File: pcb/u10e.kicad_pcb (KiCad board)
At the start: 2 copper layers, 57 parts, among them J1 MJ-4PP-9, K11 KEYSW, K12 KEYSW, K13 KEYSW, K14 KEYSW, K15 KEYSW, K16 KEYSW, K21 KEYSW, K22 KEYSW, K23 KEYSW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

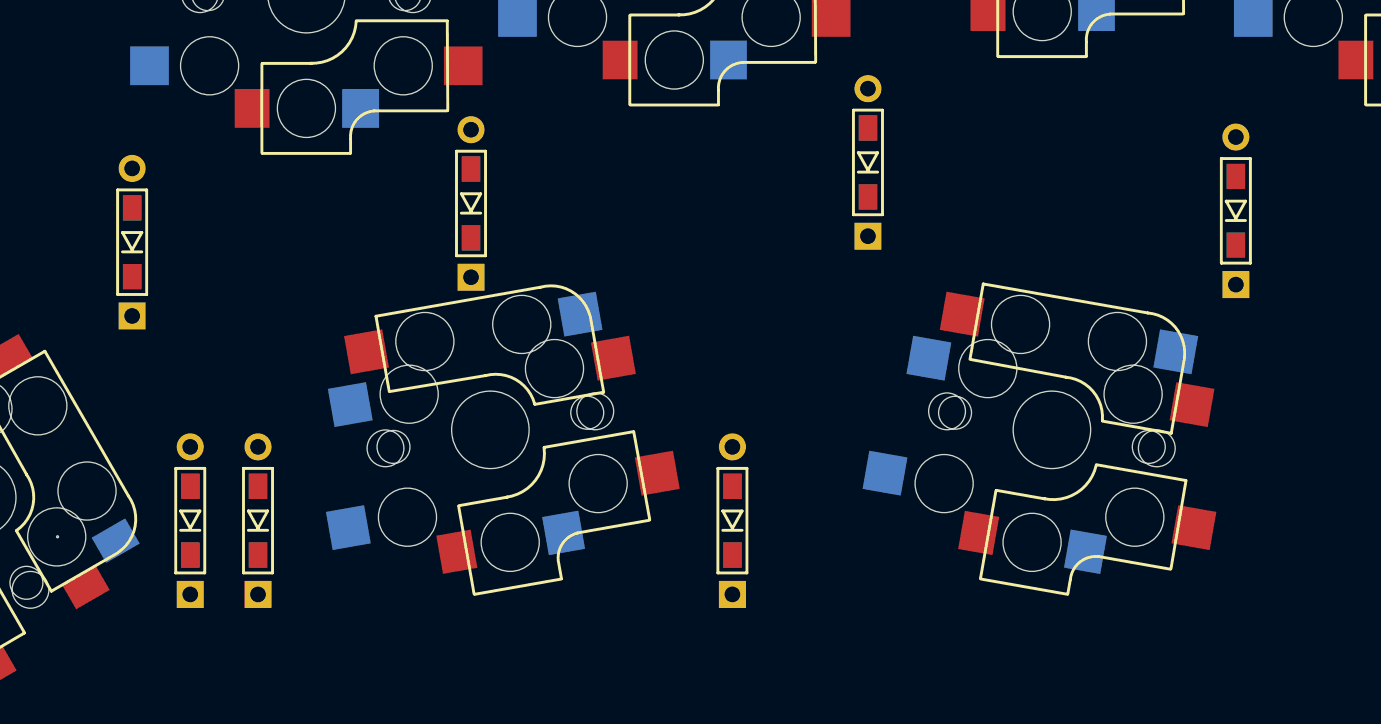
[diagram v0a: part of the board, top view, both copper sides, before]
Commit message: moved bottom row to more evenly distribute x space
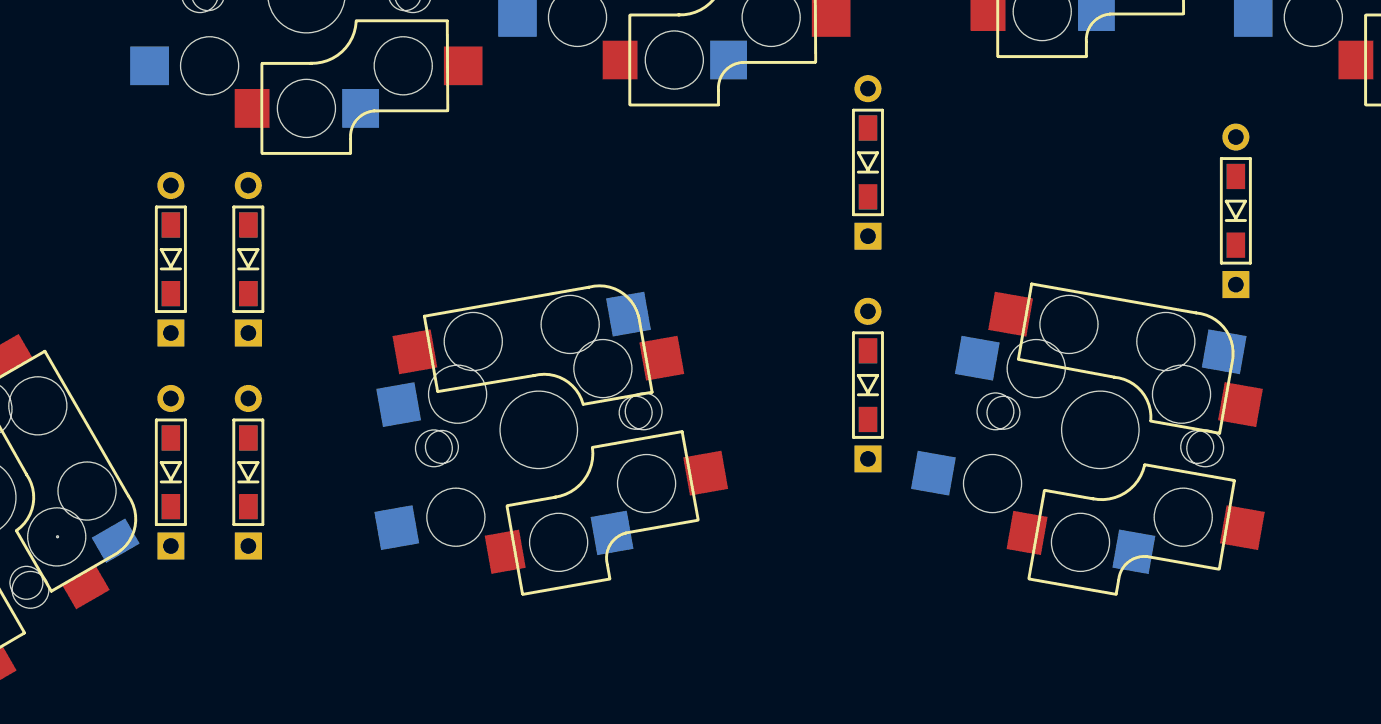
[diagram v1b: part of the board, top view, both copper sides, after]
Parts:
- moved D42 11.9 mm to (62.0, 98.7)
- moved D53 9.90 mm to (94.0, 105.2)
- moved D51 2.69 mm to (58.0, 109.7)
- moved D52 2.55 mm to (62.0, 109.7)
- moved K52 2.50 mm to (77.0, 107.5)
- moved K53 2.50 mm to (106.0, 107.5)
- moved D41 2.19 mm to (58.0, 98.7)

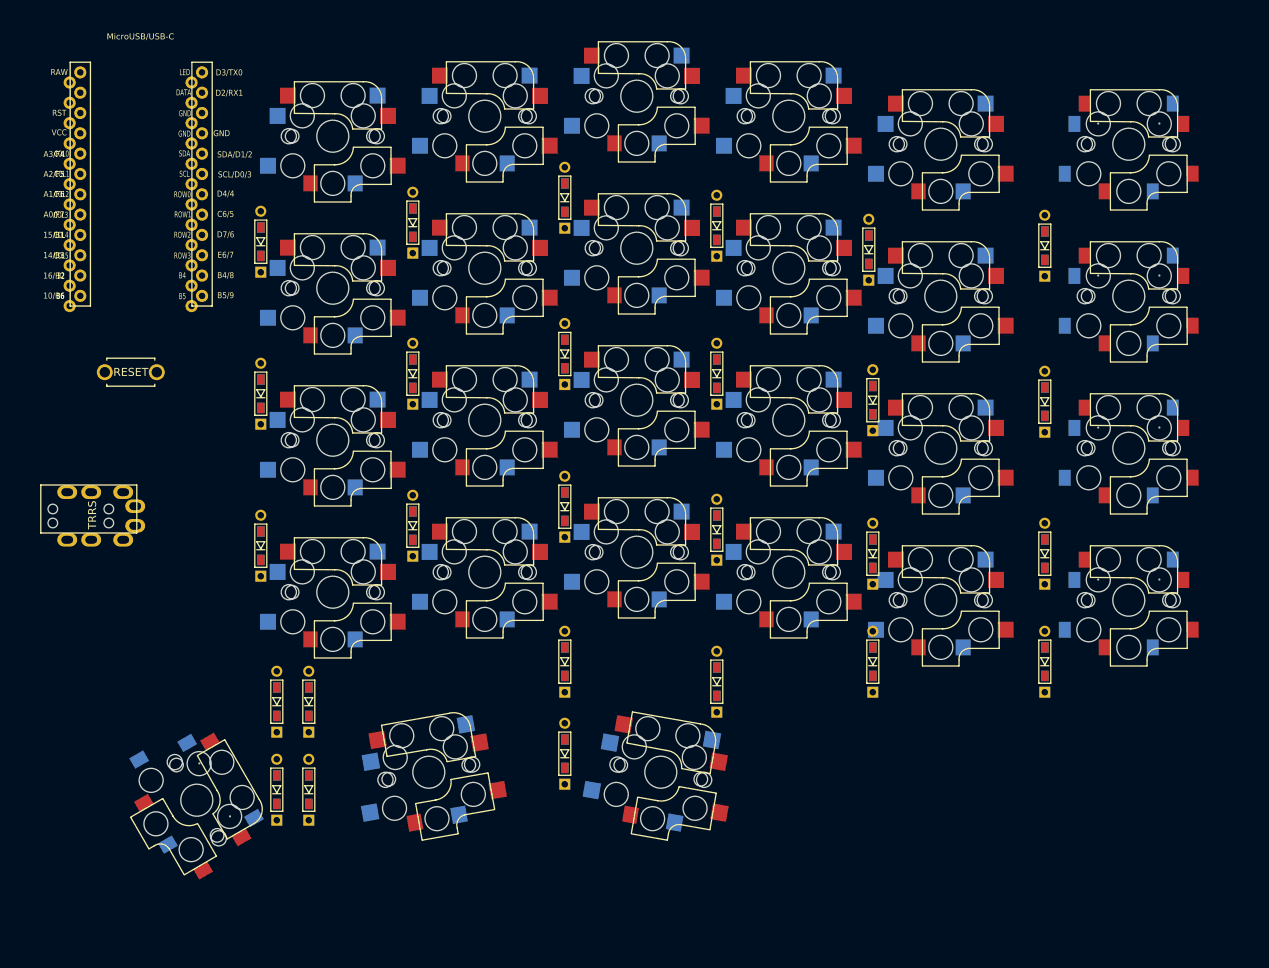
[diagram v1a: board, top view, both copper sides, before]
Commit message: added r1 edgecuts
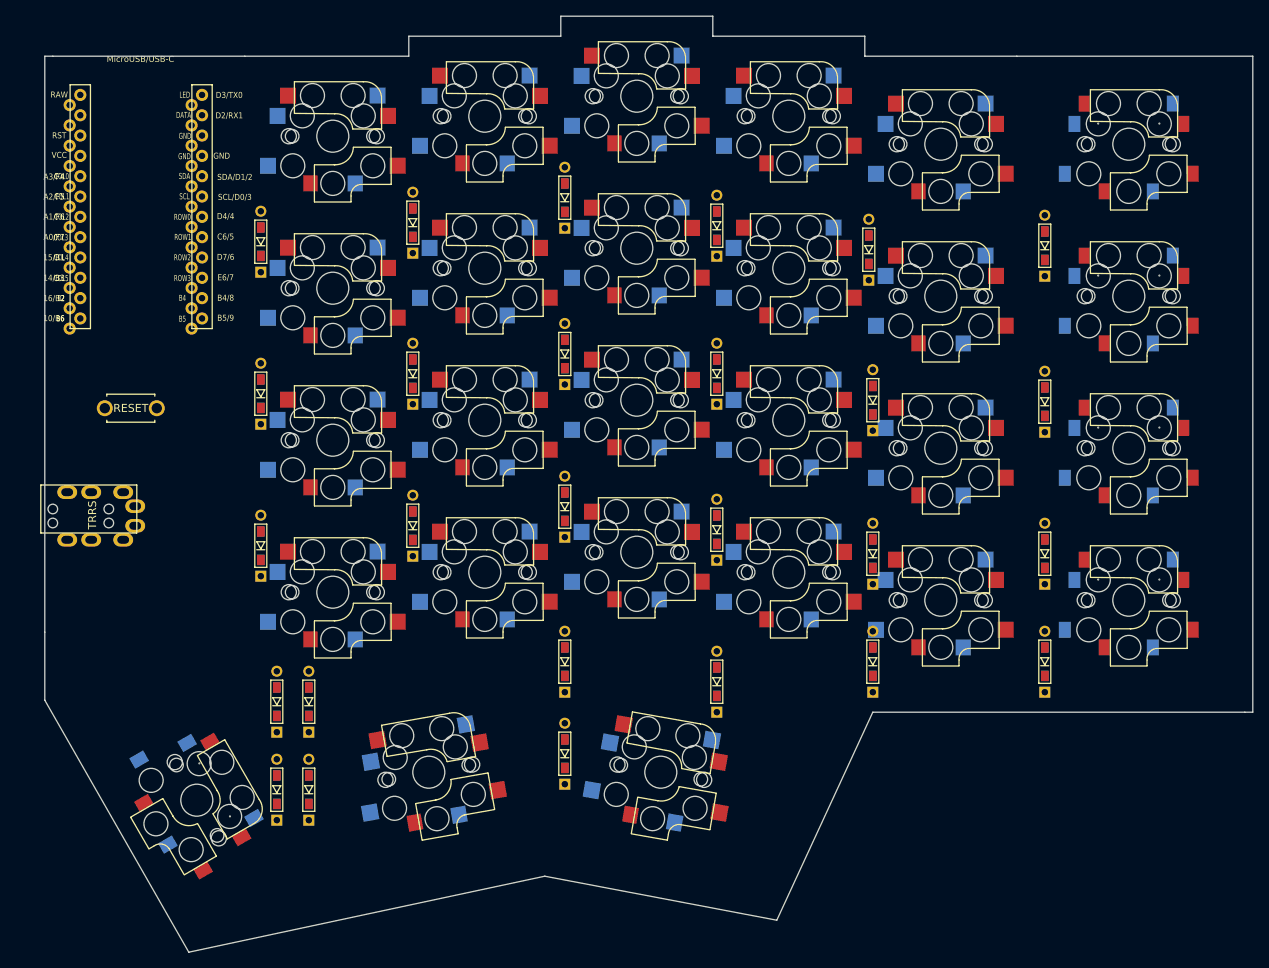
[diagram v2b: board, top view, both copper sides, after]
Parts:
- moved SW1 4.50 mm to (39.8, 62.0)
- moved U1 2.82 mm to (41.0, 37.3)
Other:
- board outline added: 151 x 117 mm
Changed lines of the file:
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@@
   (general
     (thickness 1.6)
-    (drawings 0)
+    (drawings 21)
     (tracks 0)
     (zones 0)
@@
   )
   (module kbd:ProMicro_v2 (layer F.Cu)
-    (at 41 34.5)
+    (at 41 37.318)
     (fp_text reference U1 (at 0 -5 270) (layer F.SilkS) hide
       (effects (font (size 1 1) (thickness 0.15)))
@@
   )
   (module kbd:ResetSW (layer F.Cu)
-    (at 39.75 57.5)
+    (at 39.75 62)
     (fp_text reference SW1 (at 0 2.55) (layer F.SilkS) hide
       (effects (font (size 1 1) (thickness 0.15)))
@@
     )
   )
+  (gr_line (start 29 98.5) (end 29 90) (layer Edge.Cuts) (width 0.05))
+  (gr_line (start 47 130) (end 29 98.5) (layer Edge.Cuts) (width 0.05))
+  (gr_line (start 91.5 120.5) (end 47 130) (layer Edge.Cuts) (width 0.05))
+  (gr_line (start 29 18) (end 30 18) (layer Edge.Cuts) (width 0.05))
+  (gr_line (start 29 90) (end 29 18) (layer Edge.Cuts) (width 0.05))
+  (gr_line (start 54 18) (end 30 18) (layer Edge.Cuts) (width 0.05))
+  (gr_line (start 74.5 18) (end 54 18) (layer Edge.Cuts) (width 0.05))
+  (gr_line (start 74.5 15.5) (end 74.5 18) (layer Edge.Cuts) (width 0.05))
+  (gr_line (start 93.5 15.5) (end 74.5 15.5) (layer Edge.Cuts) (width 0.05))
+  (gr_line (start 93.5 13) (end 93.5 15.5) (layer Edge.Cuts) (width 0.05))
+  (gr_line (start 112.5 13) (end 93.5 13) (layer Edge.Cuts) (width 0.05))
+  (gr_line (start 112.5 15.5) (end 112.5 13) (layer Edge.Cuts) (width 0.05))
+  (gr_line (start 131.5 15.5) (end 112.5 15.5) (layer Edge.Cuts) (width 0.05))
+  (gr_line (start 131.5 18) (end 131.5 15.5) (layer Edge.Cuts) (width 0.05))
+  (gr_line (start 150.5 18) (end 131.5 18) (layer Edge.Cuts) (width 0.05))
+  (gr_line (start 180 18) (end 150.5 18) (layer Edge.Cuts) (width 0.05))
+  (gr_line (start 180 100) (end 180 18) (layer Edge.Cuts) (width 0.05))
+  (gr_line (start 179 100) (end 180 100) (layer Edge.Cuts) (width 0.05))
+  (gr_line (start 132.5 100) (end 179 100) (layer Edge.Cuts) (width 0.05))
+  (gr_line (start 120.5 126) (end 132.5 100) (layer Edge.Cuts) (width 0.05))
+  (gr_line (start 91.5 120.5) (end 120.5 126) (layer Edge.Cuts) (width 0.05))
 )

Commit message: pre routing commit
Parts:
- moved SW1 29.1 mm to (47.8, 90.0)
- moved J1 24.7 mm to (29.8, 99.2), turned to 120 degrees
- moved D45 2.00 mm to (130.5, 93.7)
- moved U1 1.76 mm to (40.6, 35.6)
- moved D41 1.58 mm to (59.5, 99.2)
- moved D51 1.50 mm to (59.5, 109.7)
- moved K51 1.50 mm to (48.0, 112.5)
- moved D35 1.41 mm to (131.5, 79.2)
- moved D15 1.00 mm to (132.0, 41.2)
- moved D25 0.71 mm to (132.0, 60.5)
- moved D42 0.71 mm to (62.5, 99.2)
- moved D52 0.50 mm to (62.5, 109.7)
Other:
- board size 151 x 117 mm -> 151 x 115 mm

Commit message: added routes
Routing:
- net Col6: track 0.00 -> 382.8 mm, vias 0 -> 2
- net Col5: track 0.00 -> 343.7 mm, vias 0 -> 2
- net Col3: track 0.00 -> 330.3 mm, vias 0 -> 5
- net Col4: track 0.00 -> 297.0 mm, vias 0 -> 5
- net Col2: track 0.00 -> 285.3 mm, vias 0 -> 5
- net Col1: track 0.00 -> 240.3 mm, vias 0 -> 8
- net Row3: track 0.00 -> 223.1 mm
- net Row4: track 0.00 -> 201.8 mm
- net Row2: track 0.00 -> 195.8 mm, vias 0 -> 2
- net Row1: track 0.00 -> 171.6 mm
- net Row5: track 0.00 -> 160.7 mm
- net GND: track 0.00 -> 112.4 mm
- net Data: track 0.00 -> 105.3 mm
- net VCC: track 0.00 -> 86.1 mm
- net RESET: track 0.00 -> 79.5 mm
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
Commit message: Revert "added routes"
This reverts commit ca254ce08e903a7b231e3a80e900436ff372913d.
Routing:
- net Col6: track 382.8 -> 0.00 mm, vias 2 -> 0
- net Col5: track 343.7 -> 0.00 mm, vias 2 -> 0
- net Col3: track 330.3 -> 0.00 mm, vias 5 -> 0
- net Col4: track 297.0 -> 0.00 mm, vias 5 -> 0
- net Col2: track 285.3 -> 0.00 mm, vias 5 -> 0
- net Col1: track 240.3 -> 0.00 mm, vias 8 -> 0
- net Row3: track 223.1 -> 0.00 mm
- net Row4: track 201.8 -> 0.00 mm
- net Row2: track 195.8 -> 0.00 mm, vias 2 -> 0
- net Row1: track 171.6 -> 0.00 mm
- net Row5: track 160.7 -> 0.00 mm
- net GND: track 112.4 -> 0.00 mm
- net Data: track 105.3 -> 0.00 mm
- net VCC: track 86.1 -> 0.00 mm
- net RESET: track 79.5 -> 0.00 mm
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
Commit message: Added mounting holes
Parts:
- added ?: , kbd:M2_HOLE_v3, F.Cu at (54.0, 27.5)
- added ?: , kbd:M2_HOLE_v3, F.Cu at (108.5, 51.0)
- added ?: , kbd:M2_HOLE_v3, F.Cu at (34.5, 68.5)
- added ?: , kbd:M2_HOLE_v3, F.Cu at (37.0, 105.0)
- added ?: , kbd:M2_HOLE_v3, F.Cu at (89.5, 104.0)
- added ?: , kbd:M2_HOLE_v3, F.Cu at (176.0, 96.0)
- added ?: , kbd:M2_HOLE_v3, F.Cu at (175.5, 57.5)
- added ?: , kbd:M2_HOLE_v3, F.Cu at (175.5, 22.5)

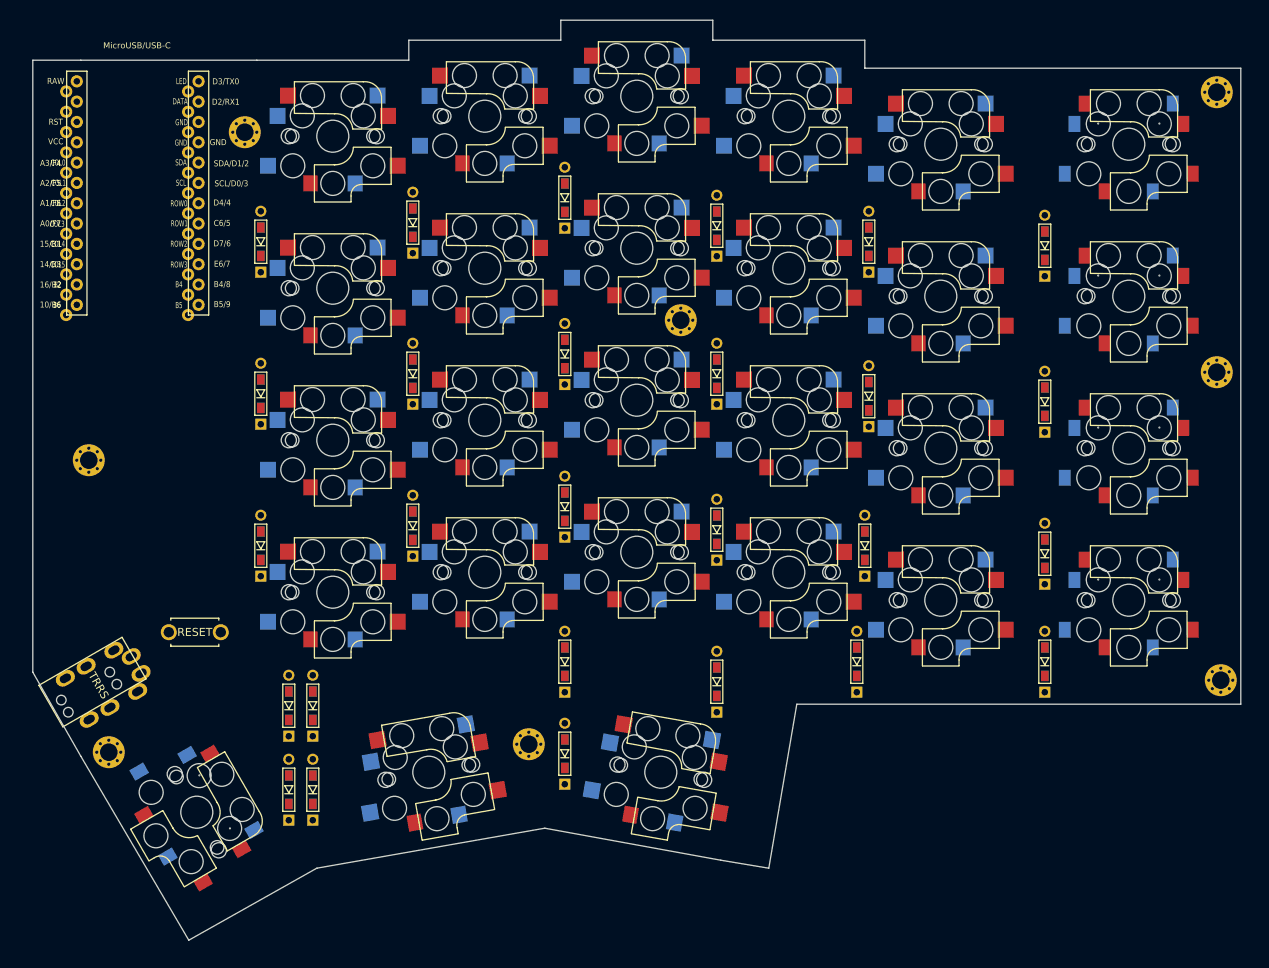
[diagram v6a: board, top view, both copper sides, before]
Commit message: Added routes and silkscreens
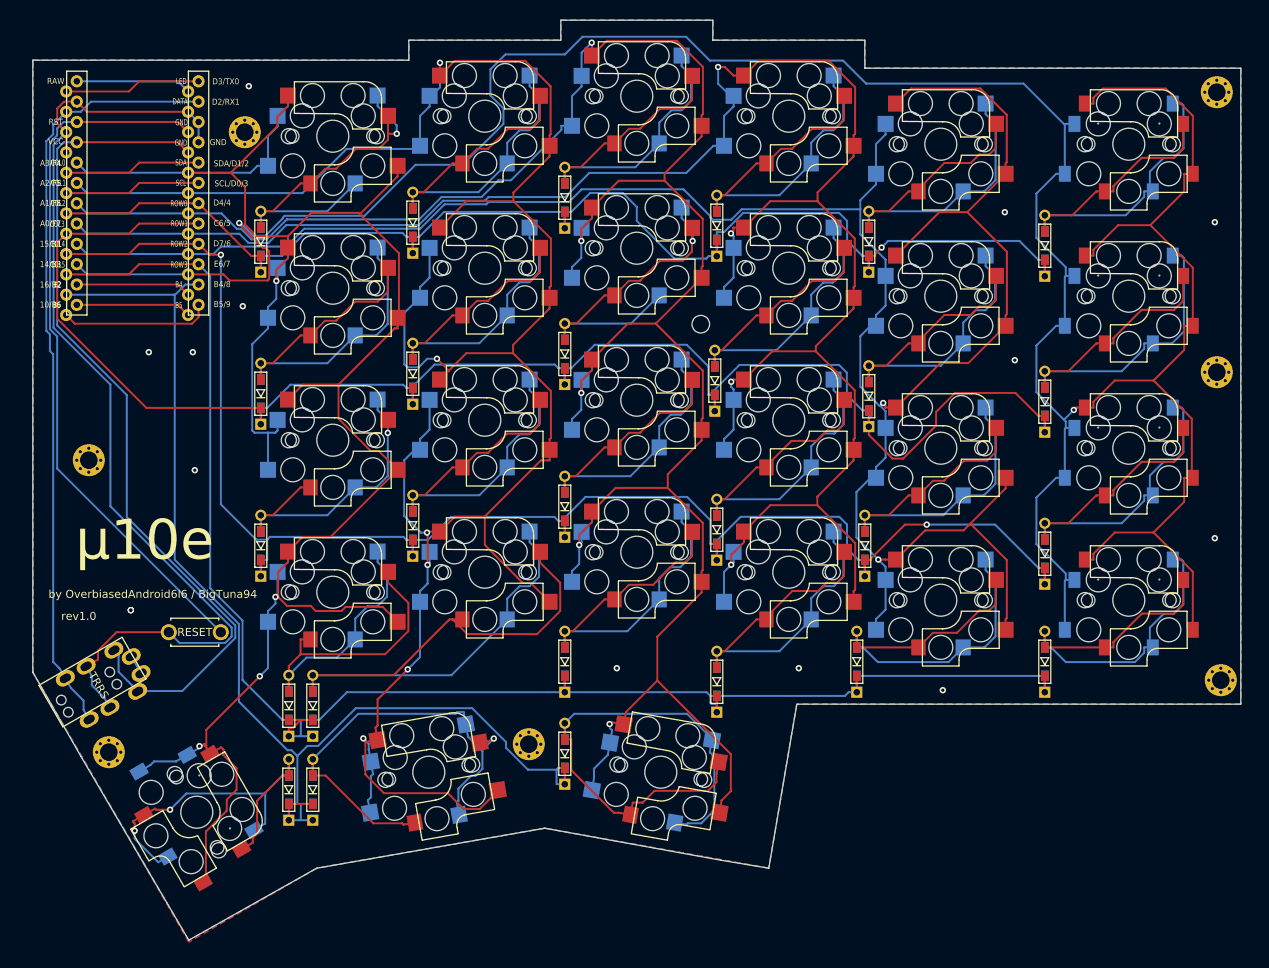
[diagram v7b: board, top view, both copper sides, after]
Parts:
- removed ? (x2): , kbd:M2_HOLE_v3
- added M3: MountingHole_2.2mm_M2, MountingHole:MountingHole_2.2mm_M2, F.Cu at (111.0, 51.5)
- added M4: , kbd:M2_HOLE_v3, F.Cu at (175.5, 57.5)
- moved D24 0.91 mm to (112.8, 58.6)
- gave numbers to parts that had none: 6
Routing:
- net Col6: track 0.00 -> 366.5 mm, vias 0 -> 2
- net Col3: track 0.00 -> 294.9 mm, vias 0 -> 5
- net Col2: track 0.00 -> 293.3 mm, vias 0 -> 6
- net Col5: track 0.00 -> 291.7 mm, vias 0 -> 2
- net Col1: track 0.00 -> 265.0 mm, vias 0 -> 4
- net Col4: track 0.00 -> 259.2 mm, vias 0 -> 4
- net Row2: track 0.00 -> 204.2 mm
- net Row4: track 0.00 -> 203.6 mm
- net Row3: track 0.00 -> 201.7 mm, vias 0 -> 2
- net Row1: track 0.00 -> 165.8 mm, vias 0 -> 1
- net Row5: track 0.00 -> 144.9 mm
- net GND: track 0.00 -> 128.0 mm, vias 0 -> 14
- net VCC: track 0.00 -> 108.9 mm
- net Data: track 0.00 -> 96.0 mm
- net Net-(D42-Pad2): track 0.00 -> 90.5 mm
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- added copper zone on B.Cu, net GND
- added copper zone on F.Cu, net GND
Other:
- board text added: "by OverbiasedAndroid6l6 / BigTuna94"
- board text added: "rev1.0"
- board text added: "μ10e"
